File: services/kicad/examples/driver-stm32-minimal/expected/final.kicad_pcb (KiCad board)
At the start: 2 copper layers, 70 x 50 mm, 27 parts, among them J1 PWR_5V, J2 SWD, J3 UART1, U1 STM32F103C8T6, U2 AMS1117-3.3, Y1 8MHz

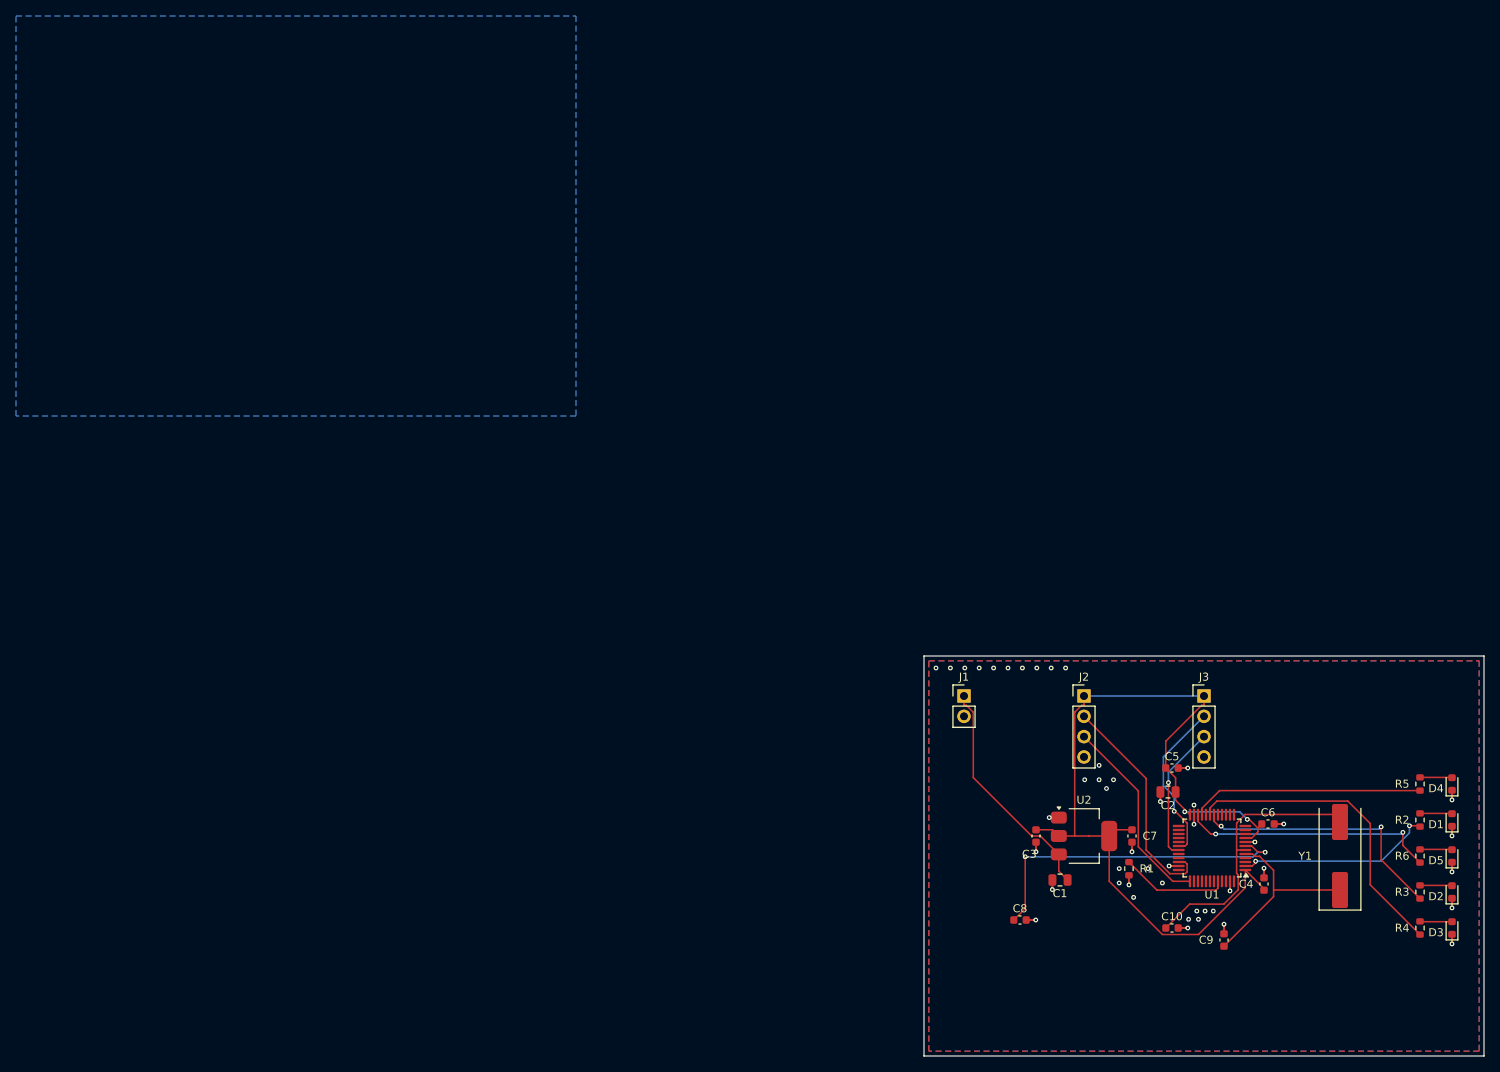
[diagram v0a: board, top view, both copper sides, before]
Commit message: banc(rejeu): douze cartes hors le banc des dix, et le trou qu elles ont revele
Demande : refaire placement et routage de toutes les cartes d `examples/`
SAUF les dix du banc, sans toucher `stm32-validation` ni `STM32-Test`.

DOUZE CARTES REJOUEES, DEUX FAMILLES.

  groupe A (input/schema.json)        regenerer_le_banc.py — garde le meilleur
      carte-11-croisements            100 % · 0 err · 0 perdu   GARDE
      driver-clignotant-ne555         100 % · 0 err · 0 perdu   GARDE
      driver-stm32-minimal            100 % · 0 err · 0 perdu   GARDE
      driver-thermometre-i2c          100 % · 0 err · 0 perdu   GARDE

  groupe B (input/circuit.json)       banc_exemples.py — ecrit dans output/
      arduino-uno       2 couches  100 %  0 manq  0 err    925 s
      esp32-baseline    2 couches  100 %  0 manq  0 err    387 s
      led-blinker       2 couches  100 %  0 manq  0 err    124 s
      nucleo-f401       4 couches   98 %  1 manq  0 err   1814 s
      stm32-baseline    2 couches  100 %  0 manq  0 err    193 s
      stm32-30          2 couches  100 %  0 manq  0 err    404 s
      stm32-60          2 couches  100 %  0 manq  0 err    414 s
      stm32-100         2 couches  100 %  0 manq  0 err    308 s

LE REJEU CONFIRME LES BOARDS LIVRES — ON NE REMPLACE RIEN.

DRC des boards VERSIONNES face aux boards du rejeu, meme instrument
(`kicad-cli pcb drc --severity-all`) des deux cotes :

      sept cartes            0 err · 0 manq des DEUX cotes   egalite
      nucleo-f401            0 manq versionne, 1 au rejeu    on garde l ancien

Livrer des boards de qualite identique ferait du bruit sans rien apporter, et
le tirage de `nucleo-f401` est moins bon : la protection a joue exactement
comme prevu.

LE TROU : CES HUIT CARTES N AVAIENT AUCUN `mesures.json`.

Leur board etait livre depuis le 2026-09-07 et RIEN ne disait ce qu il valait.
Un lecteur ne pouvait ni le verifier ni s en apercevoir — c est la faute que ce
depot poursuit partout, appliquee non pas a un compteur mais a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
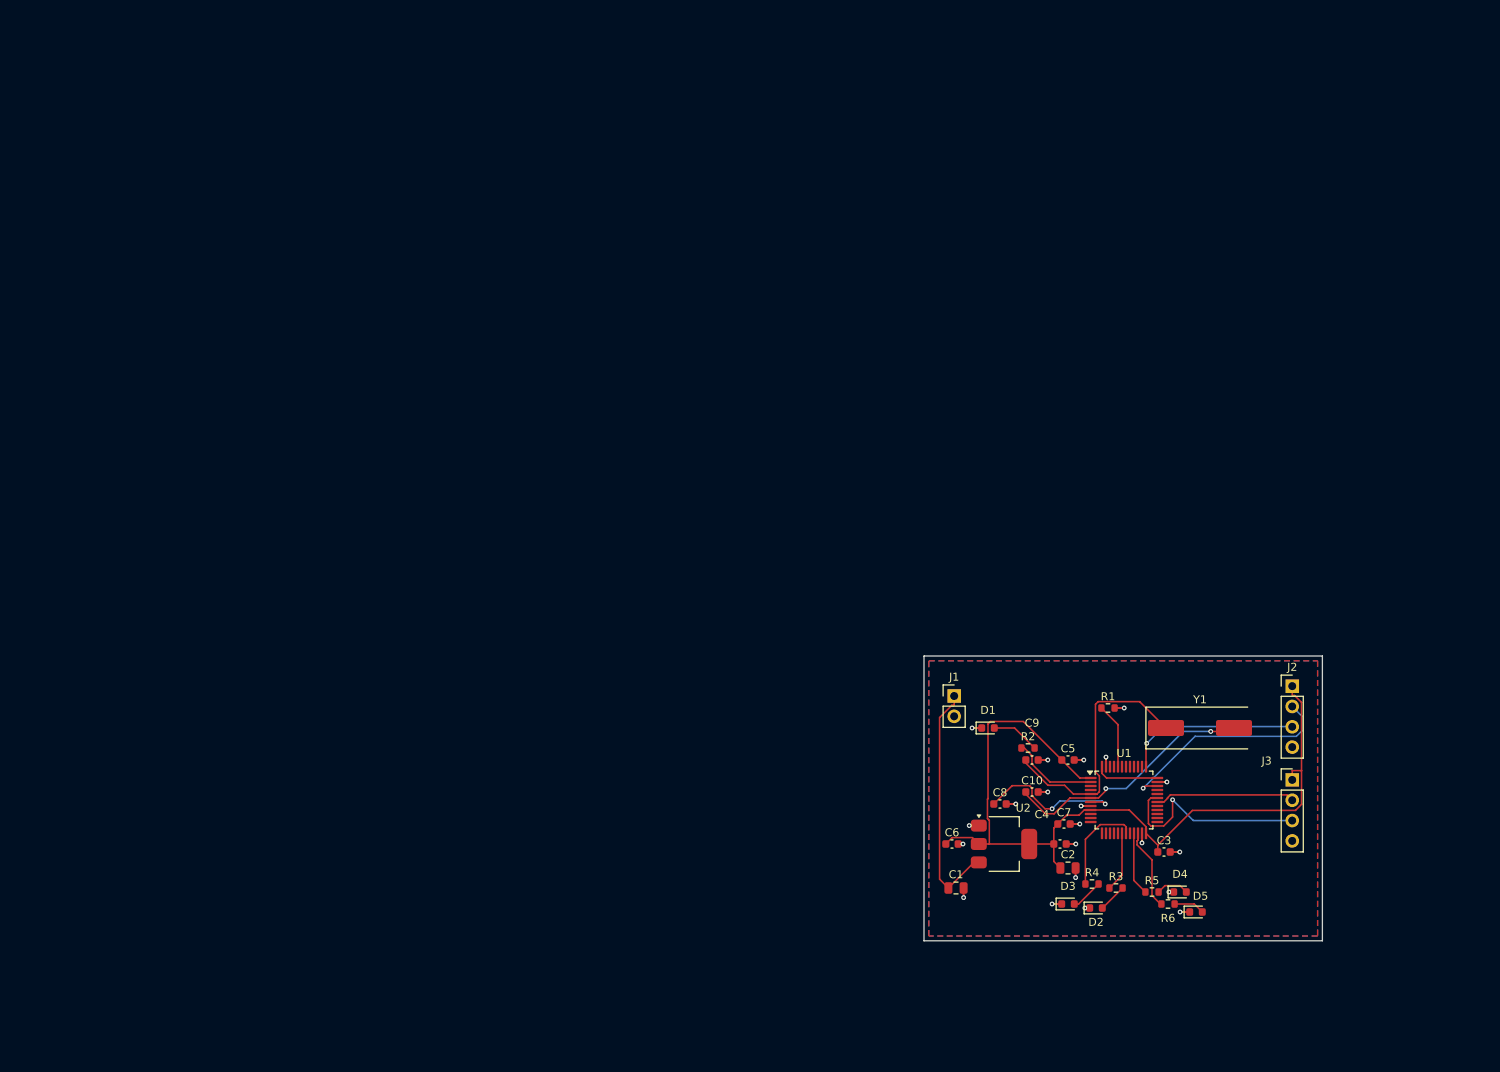
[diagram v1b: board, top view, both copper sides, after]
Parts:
- moved D1 59.1 mm to (121.5, 89.0), turned to 0 degrees
- moved R2 49.8 mm to (126.5, 91.5), turned to 0 degrees
- moved D3 48.1 mm to (131.5, 111.0), turned to 0 degrees
- moved D2 44.5 mm to (135.0, 111.5), turned to 0 degrees
- moved R4 41.4 mm to (134.5, 108.5), turned to 0 degrees
- moved C6 39.6 mm to (117.0, 103.5)
- moved R3 38.0 mm to (137.5, 109.0), turned to 0 degrees
- moved D4 36.6 mm to (145.5, 109.5), turned to 0 degrees
- moved R5 36.1 mm to (142.0, 109.5), turned to 0 degrees
- moved C9 32.9 mm to (127.0, 93.0), turned to 0 degrees
- moved D5 32.8 mm to (147.5, 112.0), turned to 0 degrees
- moved R6 32.1 mm to (144.0, 111.0), turned to 0 degrees
- moved J2 26.1 mm to (159.5, 83.8)
- moved C4 26.0 mm to (130.5, 103.5), turned to 0 degrees
- moved C10 24.4 mm to (127.0, 97.0)
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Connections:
- U1 pad 36: Net-(U1-36) -> PWR_FLAG
- U1 pad 48: Net-(U1-48) -> PWR_FLAG
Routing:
- net LED_PB1: track 38.8 -> 12.4 mm
- net LED_PB0: track 33.2 -> 7.49 mm, vias 2 -> 0
- net NRST: track 41.5 -> 19.1 mm
- net LED_PB11: track 31.9 -> 10.2 mm, vias 2 -> 0
- net LED_PB10: track 29.0 -> 7.95 mm
- net LED_PC13: track 24.6 -> 11.0 mm, vias 2 -> 0
- net UART1_RX: track 17.0 -> 25.9 mm
- net OSC_IN: track 24.7 -> 32.7 mm
- net PWR_FLAG: track 0.00 -> 7.99 mm
- net +3V3: track 110.9 -> 105.4 mm, vias 2 -> 0
- net BOOT0: track 13.5 -> 8.20 mm
- net UART1_TX: track 20.5 -> 17.6 mm, vias 1 -> 0
- net SWCLK: track 24.8 -> 22.0 mm, vias 0 -> 1
- net OSC_OUT: track 34.3 -> 31.9 mm, vias 0 -> 2
- net D1_A: track 4.02 -> 6.07 mm
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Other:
- board size 70 x 50 mm -> 49.8 x 35.6 mm
